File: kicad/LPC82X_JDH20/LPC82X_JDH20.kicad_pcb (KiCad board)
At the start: 2 copper layers, 2 parts

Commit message: started initial PCB layout
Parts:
- added C1: 10u, SquantorRcl:C_0805, F.Cu at (130.4, 91.9)
- added C2: 18p, SquantorRcl:C_0402, F.Cu at (155.9, 119.0)
- added C3: 1u, SquantorRcl:C_0603, F.Cu at (152.1, 113.6)
- added C4: 1u, SquantorRcl:C_0603, F.Cu at (152.1, 112.1)
- added C5: 18p, SquantorRcl:C_0402, F.Cu at (155.9, 117.7)
- added C6: 100n, SquantorRcl:C_0402, F.Cu at (160.1, 114.2)
- added C7: 100n, SquantorRcl:C_0402, F.Cu at (155.9, 116.5)
- added FB1: FB, SquantorRcl:C_0402, F.Cu at (153.6, 119.1)
- added FB2: FB, SquantorRcl:C_0402, F.Cu at (160.1, 113.0)
- added FB3: FB, SquantorRcl:C_0402, F.Cu at (153.6, 117.8)
- added J1: Conn_01x09, SquantorConnectors:Header-0254-1X09-H010, F.Cu at (127.0, 101.6)
- added J2: JTAG_2X05, SquantorConnectors:Header-0127-2X05-H006, F.Cu at (136.1, 91.7)
- added J3: Conn_01x09, SquantorConnectors:Header-0254-1X09-H010, F.Cu at (142.2, 101.6)
- added M1: LPC824M201JDH20, SquantorIC:SOT360, F.Cu at (134.6, 101.6)
- added R1: 100K, SquantorRcl:R_0402_hand, F.Cu at (133.0, 95.3)
- added R2: 100k, SquantorRcl:R_0402_hand, F.Cu at (150.5, 115.1)
- added R3: 100k, SquantorRcl:R_0402_hand, F.Cu at (139.2, 96.1)
- added R4: 100, SquantorRcl:R_0402_hand, F.Cu at (157.8, 113.0)
- added R5: 100, SquantorRcl:R_0402_hand, F.Cu at (157.8, 114.4)
- added R6: 100, SquantorRcl:R_0402_hand, F.Cu at (133.0, 94.0)
- added SJ1: SolderJumper_2way_1conn, SquantorSpecial:solder_jumper_2way_conn, F.Cu at (158.1, 115.7)
- added Y1: 12MHz, SquantorCrystal:Crystal_3225_4, F.Cu at (132.1, 110.5)
- N2: value 20180910 -> 20181104
- moved N1 13.0 mm to (160.7, 103.5)
- moved N2 13.0 mm to (161.6, 107.3)
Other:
- board outline added: 18.7 x 23.8 mm

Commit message: initial component placement
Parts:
- N1: moved to B.Cu
- N2: value 20181104 -> 20181110; moved to B.Cu
- moved R5 29.2 mm to (136.8, 94.0)
- moved C6 27.6 mm to (133.4, 107.1)
- moved C2 27.2 mm to (130.0, 110.6)
- moved R4 26.2 mm to (139.4, 94.3)
- moved R2 24.9 mm to (135.4, 95.3)
- moved C5 23.5 mm to (133.5, 110.6)
- moved C7 22.3 mm to (135.7, 107.0)
- moved FB2 22.0 mm to (138.2, 111.2), turned to 90 degrees
- moved FB1 19.4 mm to (135.8, 111.2), turned to 90 degrees
- moved SJ1 19.3 mm to (139.2, 112.0)
- moved C3 18.7 mm to (134.1, 108.5)
- moved FB3 17.8 mm to (137.0, 111.3), turned to 90 degrees
- moved C4 16.1 mm to (136.4, 108.6)
- moved N1 5.19 mm to (161.3, 108.7), turned to 180 degrees
- moved N2 4.97 mm to (161.3, 112.3)

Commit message: component placement done
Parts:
- moved N1 27.8 mm to (134.5, 101.3)
- moved N2 27.8 mm to (134.5, 104.9)
- moved C2 3.65 mm to (130.6, 107.0), turned to 180 degrees
- moved C5 3.45 mm to (130.5, 112.3)
- moved R3 3.20 mm to (136.1, 95.3), turned to 180 degrees
- moved R2 3.00 mm to (138.4, 95.3), turned to 180 degrees
- moved FB2 2.30 mm to (136.3, 109.9), turned to 270 degrees
- moved FB1 1.81 mm to (134.6, 109.9), turned to 270 degrees
- moved Y1 1.68 mm to (130.6, 109.7), turned to 270 degrees
- moved SJ1 1.60 mm to (139.1, 110.4), turned to 180 degrees
- moved FB3 1.49 mm to (137.5, 109.9), turned to 270 degrees
- moved C6 1.21 mm to (134.5, 106.6)
- moved C7 1.17 mm to (136.8, 106.6)
- moved R4 1.04 mm to (138.4, 94.0), turned to 180 degrees
- moved C4 0.92 mm to (137.1, 108.0)
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
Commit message: intermediate layout checkin
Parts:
- moved C1 9.20 mm to (139.6, 92.1)
- moved J2 2.90 mm to (133.2, 91.7)
- moved R1 2.90 mm to (130.9, 95.3)
- moved R2 2.90 mm to (135.5, 95.3)
- moved R3 2.90 mm to (133.2, 95.3)
- moved R4 2.90 mm to (135.5, 94.0)
- moved R5 2.90 mm to (133.2, 94.0)
- moved R6 2.90 mm to (130.9, 94.0)
- moved C2 0.71 mm to (130.7, 107.7), turned to 0 degrees
- moved Y1 0.32 mm to (130.7, 110.0), turned to 0 degrees
- moved C5 0.30 mm to (130.8, 112.3), turned to 180 degrees
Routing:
- net /PIO0_9: track 0.00 -> 11.4 mm
- net /PIO0_4: track 0.00 -> 10.3 mm
- net /PIO0_3: track 0.00 -> 9.62 mm
- net /PIO0_2: track 0.00 -> 9.31 mm
- net VSS: track 0.00 -> 8.46 mm, vias 0 -> 3
- net /PIO0_1: track 0.00 -> 8.20 mm
- net /PIO0_11: track 0.00 -> 7.93 mm
- net /PIO0_10: track 0.00 -> 7.82 mm
- net VDD: track 0.00 -> 6.66 mm
- net /PIO0_15: track 0.00 -> 5.49 mm
- net Net-(J2-Pad4): track 0.00 -> 2.20 mm
- net Net-(J2-Pad10): track 0.00 -> 1.79 mm
- net Net-(J2-Pad2): track 0.00 -> 1.79 mm
- net /RESET: track 0.00 -> 1.30 mm
- added copper zone on B.Cu, net VSS
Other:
- rule pad_to_mask_clearance: 0.2 -> 0.1

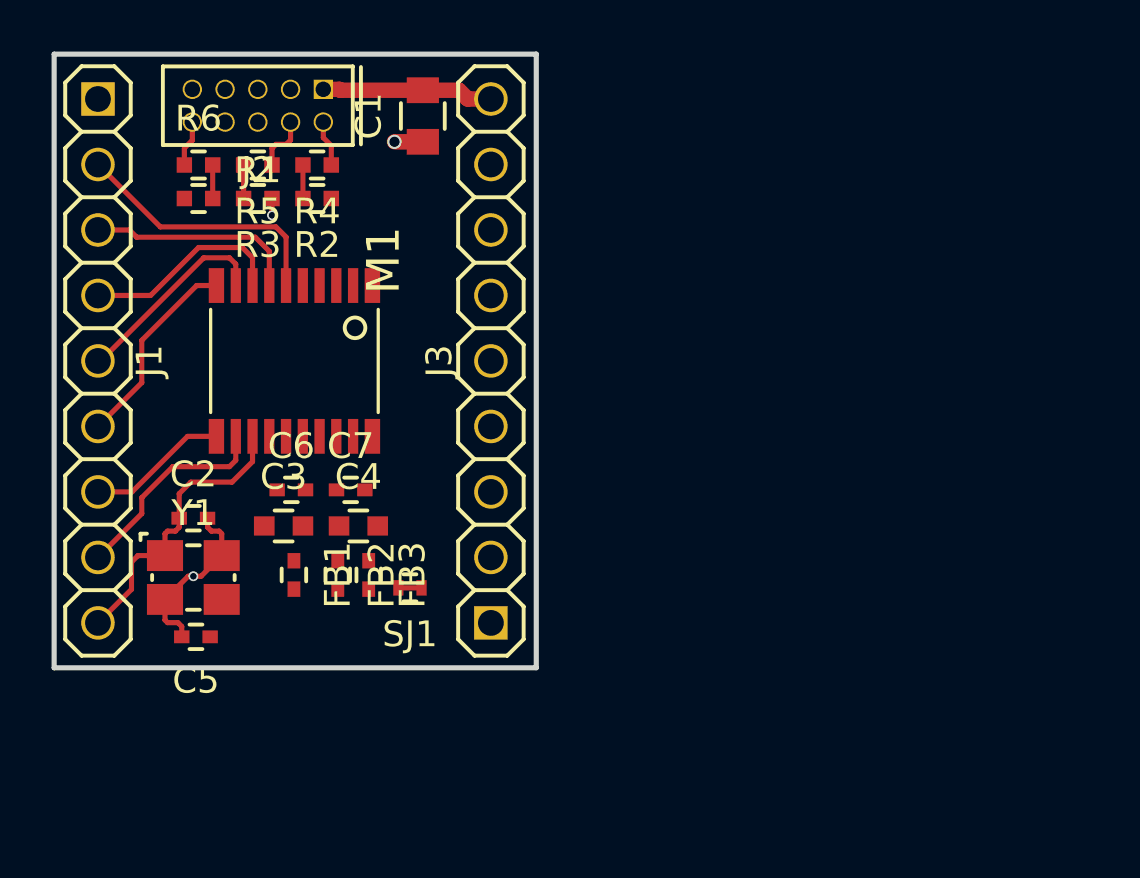
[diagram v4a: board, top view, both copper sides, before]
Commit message: layout done, positioning silk labels
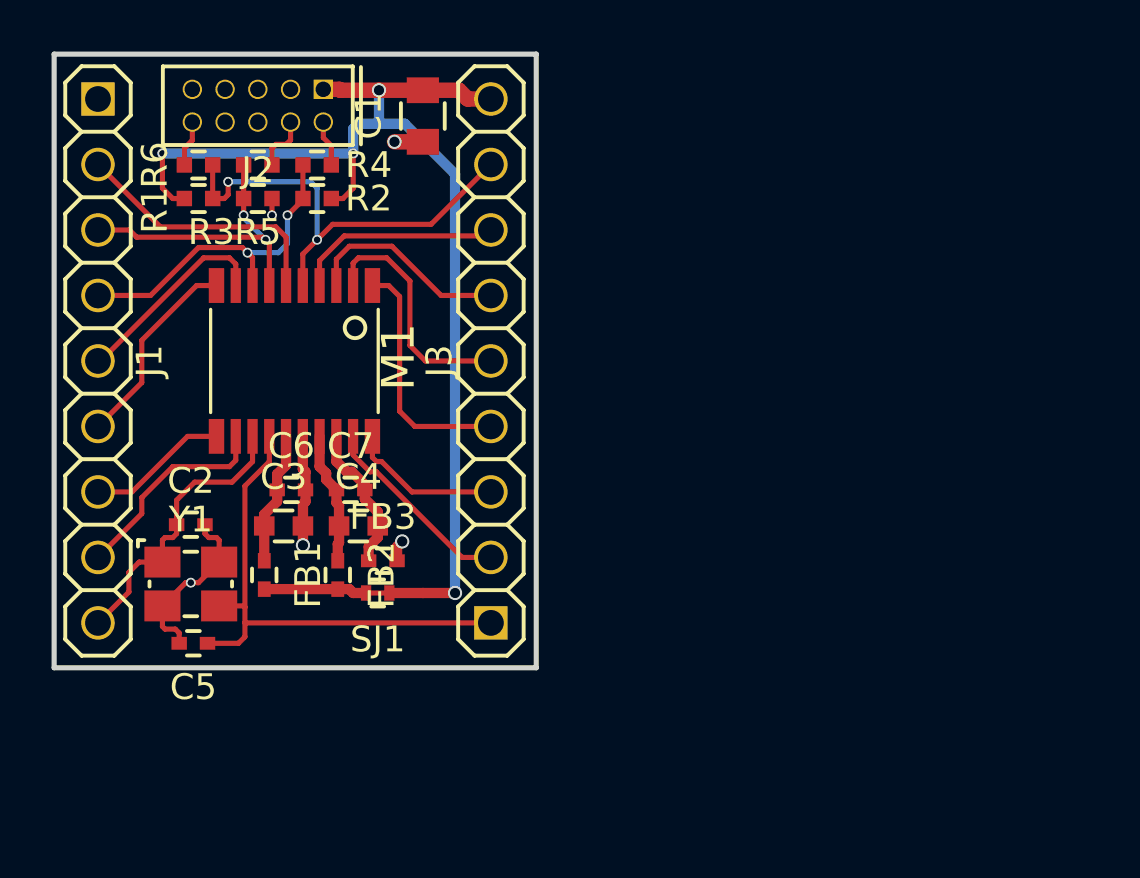
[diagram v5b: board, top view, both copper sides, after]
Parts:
- moved SJ1 1.27 mm to (137.8, 110.6)
- moved FB1 1.15 mm to (133.4, 109.9)
- moved FB3 0.78 mm to (138.1, 109.3), turned to 0 degrees
- moved C5 0.27 mm to (130.7, 112.5)
- moved C2 0.27 mm to (130.6, 108.0)
- moved Y1 0.27 mm to (130.6, 110.2)
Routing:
- net VDD: track 6.66 -> 44.7 mm, vias 0 -> 4
- net /PIO0_8: track 0.00 -> 20.3 mm
- net /RESET: track 1.30 -> 18.0 mm, vias 0 -> 2
- net /PIO0_23: track 0.00 -> 9.47 mm
- net /PIO0_17: track 0.00 -> 9.42 mm
- net /PIO0_12: track 0.00 -> 8.11 mm
- net /PIO0_13: track 0.00 -> 8.02 mm
- net /PIO0_0: track 0.00 -> 7.71 mm
- net /PIO0_14: track 0.00 -> 5.97 mm
- net Net-(C4-Pad2): track 0.00 -> 5.75 mm
- net Net-(C3-Pad1): track 0.00 -> 5.18 mm
- net Net-(C4-Pad1): track 0.00 -> 5.16 mm
- net VSS: track 8.46 -> 13.6 mm, vias 3 -> 5
- net Net-(FB1-Pad2): track 0.00 -> 4.01 mm
- net /PIO0_2: track 9.31 -> 13.0 mm, vias 0 -> 2
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
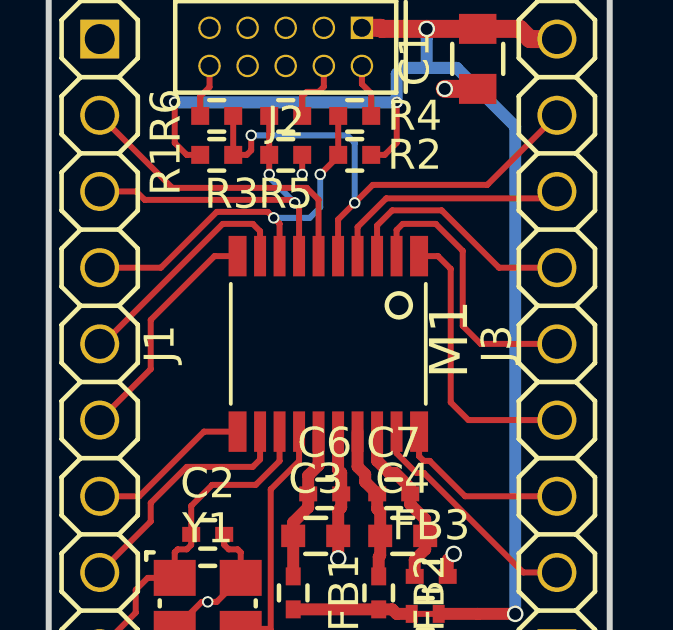
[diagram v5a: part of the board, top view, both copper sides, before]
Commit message: updated to new component
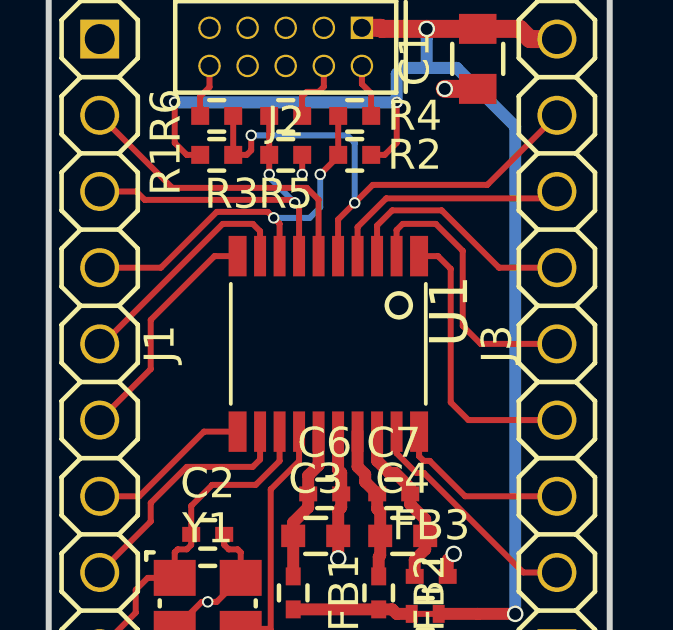
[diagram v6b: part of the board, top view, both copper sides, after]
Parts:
- removed M1: LPC824M201JDH20, SquantorIC:SOT360
- added U1: LPC824M201JDH20, SquantorIC:SOT360, F.Cu at (134.6, 101.6)
